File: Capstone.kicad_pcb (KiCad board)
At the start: 2 copper layers, 21 parts, among them U1 XIAO-ESP32-S3-DIP, U11 SN74HC161DR, U3 74LS151

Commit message: Redo Base Project file add code
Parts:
- removed C1: C, Capacitor_SMD:CP_Elec_3x5.3
- removed R1, R10, R11, R12, R13, R14, R15, R16, R17, R2, R3, R4, R5, R6, R7, R8, R9: R, Resistor_SMD:R_0201_0603Metric_Pad0.64x0.40mm_HandSolder
- removed U11: SN74HC161DR, CapstoneFootprints:D16
- added Cf1: 10p, Capacitor_THT:C_Disc_D3.8mm_W2.6mm_P2.50mm, F.Cu at (153.3, 105.8)
- added Cf2: 10p, Capacitor_THT:C_Disc_D3.8mm_W2.6mm_P2.50mm, F.Cu at (153.3, 110.0)
- added Cf3: 10p, Capacitor_THT:C_Disc_D3.8mm_W2.6mm_P2.50mm, F.Cu at (161.0, 105.8)
- added Cf4: 10p, Capacitor_THT:C_Disc_D3.8mm_W2.6mm_P2.50mm, F.Cu at (161.0, 110.0)
- added Ra1: 100k, Resistor_THT:R_Axial_DIN0204_L3.6mm_D1.6mm_P5.08mm_Horizontal, F.Cu at (142.3, 70.4)
- added Ra2: 100k, Resistor_THT:R_Axial_DIN0204_L3.6mm_D1.6mm_P5.08mm_Horizontal, F.Cu at (142.3, 92.3)
- added Rb1: 100k, Resistor_THT:R_Axial_DIN0204_L3.6mm_D1.6mm_P5.08mm_Horizontal, F.Cu at (142.3, 73.6)
- added Rb2: 100k, Resistor_THT:R_Axial_DIN0204_L3.6mm_D1.6mm_P5.08mm_Horizontal, F.Cu at (142.3, 95.4)
- added Rc1: 100k, Resistor_THT:R_Axial_DIN0204_L3.6mm_D1.6mm_P5.08mm_Horizontal, F.Cu at (142.3, 76.7)
- added Rc2: 100k, Resistor_THT:R_Axial_DIN0204_L3.6mm_D1.6mm_P5.08mm_Horizontal, F.Cu at (142.3, 98.6)
- added Rd1: 100k, Resistor_THT:R_Axial_DIN0204_L3.6mm_D1.6mm_P5.08mm_Horizontal, F.Cu at (142.3, 79.9)
- added Rd2: 100k, Resistor_THT:R_Axial_DIN0204_L3.6mm_D1.6mm_P5.08mm_Horizontal, F.Cu at (142.3, 101.7)
- added Rf1: 100k, Resistor_THT:R_Axial_DIN0204_L3.6mm_D1.6mm_P5.08mm_Horizontal, F.Cu at (142.3, 83.0)
- added Rf2: 100k, Resistor_THT:R_Axial_DIN0204_L3.6mm_D1.6mm_P5.08mm_Horizontal, F.Cu at (142.3, 86.2)
- added Rf3: 100k, Resistor_THT:R_Axial_DIN0204_L3.6mm_D1.6mm_P5.08mm_Horizontal, F.Cu at (142.3, 104.9)
- added Rf4: 100k, Resistor_THT:R_Axial_DIN0204_L3.6mm_D1.6mm_P5.08mm_Horizontal, F.Cu at (142.3, 108.0)
- added U2: LM358, Package_DIP:DIP-8_W7.62mm, F.Cu at (150.4, 70.9)
- added U4: LM358, Package_DIP:DIP-8_W7.62mm, F.Cu at (150.4, 92.7)
- added U5: LM358, Package_DIP:DIP-8_W7.62mm, F.Cu at (161.2, 92.7)
- U3: value 74LS151 -> LM358; footprint CapstoneFootprints:D16 -> Package_DIP:DIP-8_W7.62mm
- moved U3 15.1 mm to (161.2, 70.9)
- moved U1 6.13 mm to (184.0, 80.5), turned to 90 degrees
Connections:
- U1 pad 1: /Filter/Vout -> /SensorReader/Vout
- U1 pad 13: GND -> /SensorReader/Vref
- U1 pad 14: /8xAmplifier/V+ -> /SensorReader/V+
- U1 pad 2: unconnected-(U1-GPIO2_A1_D1-Pad2) -> /SensorReader1/Vout
- U1 pad 6: Net-(U1-GPIO6_A5_D5_SCL) -> unconnected-(U1-GPIO6_A5_D5_SCL-Pad6)
- U3 pad 1: /8xAmplifier/Vout4 -> /SensorReader1/Vout
- U3 pad 2: /8xAmplifier/Vout3 -> Net-(U3A--)
- U3 pad 3: /8xAmplifier/Vout2 -> Net-(U3A-+)
- U3 pad 4: /8xAmplifier/Vout1 -> /SensorReader/V-
- U3 pad 5: /Filter/Vin -> unconnected-(U3B-+-Pad5)
- U3 pad 8: GND -> /SensorReader/V+

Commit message: PCB designed rev1.0
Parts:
- removed Ra1, Ra2, Rb1, Rb2, Rd1, Rd2: 100k, Resistor_THT:R_Axial_DIN0204_L3.6mm_D1.6mm_P5.08mm_Horizontal
- added BT1: Battery, Connector_JST:JST_SUR_BM02B-SURS-TF_1x02-1MP_P0.80mm_Vertical, F.Cu at (176.7, 125.5)
- added C1: 100p, Capacitor_THT:C_Disc_D3.8mm_W2.6mm_P2.50mm, F.Cu at (95.6, 120.5)
- added C10: 1uF, Capacitor_THT:C_Disc_D3.8mm_W2.6mm_P2.50mm, F.Cu at (172.1, 105.4)
- added C11: 2.2uF, Capacitor_THT:C_Disc_D3.8mm_W2.6mm_P2.50mm, F.Cu at (166.8, 99.5)
- added C12: 100nF, Capacitor_THT:C_Disc_D3.8mm_W2.6mm_P2.50mm, F.Cu at (186.0, 126.2)
- added C13: 100p, Capacitor_THT:C_Disc_D3.8mm_W2.6mm_P2.50mm, F.Cu at (91.4, 123.7)
- added C14: 100p, Capacitor_THT:C_Disc_D3.8mm_W2.6mm_P2.50mm, F.Cu at (86.6, 123.7)
- added C16: 100p, Capacitor_THT:C_Disc_D3.8mm_W2.6mm_P2.50mm, F.Cu at (95.7, 103.7)
- added C17: 100p, Capacitor_THT:C_Disc_D3.8mm_W2.6mm_P2.50mm, F.Cu at (91.4, 106.9)
- added C18: 100p, Capacitor_THT:C_Disc_D3.8mm_W2.6mm_P2.50mm, F.Cu at (86.6, 106.9)
- added C19: 10uF, Capacitor_THT:C_Disc_D3.8mm_W2.6mm_P2.50mm, F.Cu at (177.4, 117.2)
- added C3: 3900pF, Capacitor_THT:C_Disc_D3.8mm_W2.6mm_P2.50mm, F.Cu at (177.4, 106.8)
- added C4: 10pF, Capacitor_THT:C_Disc_D3.8mm_W2.6mm_P2.50mm, F.Cu at (174.9, 120.6)
- added C5: 4.7uF, Capacitor_THT:C_Disc_D3.8mm_W2.6mm_P2.50mm, F.Cu at (147.9, 118.4)
- added C6: 10uF, Capacitor_THT:C_Disc_D3.8mm_W2.6mm_P2.50mm, F.Cu at (186.0, 121.5)
- added C7: 1uF, Capacitor_THT:C_Disc_D3.8mm_W2.6mm_P2.50mm, F.Cu at (179.8, 110.2)
- added C8: 10nF, Capacitor_THT:C_Disc_D3.8mm_W2.6mm_P2.50mm, F.Cu at (179.8, 106.8)
- added C9: 10uF, Capacitor_THT:C_Disc_D3.8mm_W2.6mm_P2.50mm, F.Cu at (186.0, 114.2)
- added D1: LED, LED_THT:LED_D3.0mm_Horizontal_O1.27mm_Z6.0mm, F.Cu at (163.9, 120.8)
- added D2: LED, LED_THT:LED_D3.0mm_Horizontal_O1.27mm_Z6.0mm, F.Cu at (169.9, 120.8)
- added D3: 1N34A, Diode_THT:D_DO-35_SOD27_P2.54mm_Vertical_AnodeUp, F.Cu at (96.7, 124.0)
- added D4: 1N34A, Diode_THT:D_DO-35_SOD27_P2.54mm_Vertical_AnodeUp, F.Cu at (96.7, 107.2)
- added D5: B240A, Diode_SMD:D_SMA, F.Cu at (178.6, 98.4)
- added J1: USB_C_Receptacle_PowerOnly_6P, Connector_USB:USB_C_Receptacle_GCT_USB4135-GF-A_6P_TopMnt_Horizontal, F.Cu at (156.0, 124.4)
- added L1: 3.9uH, Inductor_SMD:L_Bourns-SRN4018, F.Cu at (181.2, 121.2)
- added R1: 4.75k, Resistor_THT:R_Axial_DIN0204_L3.6mm_D1.6mm_P5.08mm_Horizontal, F.Cu at (174.9, 109.4)
- added R10: 1k, Resistor_THT:R_Axial_DIN0204_L3.6mm_D1.6mm_P5.08mm_Horizontal, F.Cu at (186.4, 111.9)
- added R11: 1k, Resistor_THT:R_Axial_DIN0204_L3.6mm_D1.6mm_P5.08mm_Horizontal, F.Cu at (142.8, 120.6)
- added R12: 500, Resistor_THT:R_Axial_DIN0204_L3.6mm_D1.6mm_P5.08mm_Horizontal, F.Cu at (111.4, 120.6)
- added R13: 500, Resistor_THT:R_Axial_DIN0204_L3.6mm_D1.6mm_P5.08mm_Horizontal, F.Cu at (111.4, 103.8)
- added R14: 1k, Resistor_THT:R_Axial_DIN0204_L3.6mm_D1.6mm_P5.08mm_Horizontal, F.Cu at (142.9, 103.8)
- added R15: 100R, Resistor_THT:R_Axial_DIN0204_L3.6mm_D1.6mm_P5.08mm_Horizontal, F.Cu at (186.4, 104.7)
- added R2: 33.2K, Resistor_THT:R_Axial_DIN0204_L3.6mm_D1.6mm_P5.08mm_Horizontal, F.Cu at (177.2, 114.6)
- added R3: 5.11k, Resistor_THT:R_Axial_DIN0204_L3.6mm_D1.6mm_P5.08mm_Horizontal, F.Cu at (157.9, 118.4)
- added R4: 5.11k, Resistor_THT:R_Axial_DIN0204_L3.6mm_D1.6mm_P5.08mm_Horizontal, F.Cu at (147.8, 121.3)
- added R5: 102k, Resistor_THT:R_Axial_DIN0204_L3.6mm_D1.6mm_P5.08mm_Horizontal, F.Cu at (173.8, 102.7)
- added R6: 1, Resistor_THT:R_Axial_DIN0204_L3.6mm_D1.6mm_P5.08mm_Horizontal, F.Cu at (179.8, 117.9)
- added R7: 5.11k, Resistor_THT:R_Axial_DIN0204_L3.6mm_D1.6mm_P5.08mm_Horizontal, F.Cu at (163.7, 118.0)
- added R8: 5.11k, Resistor_THT:R_Axial_DIN0204_L3.6mm_D1.6mm_P5.08mm_Horizontal, F.Cu at (171.0, 118.2)
- added R9: 5.11k, Resistor_THT:R_Axial_DIN0204_L3.6mm_D1.6mm_P5.08mm_Horizontal, F.Cu at (171.0, 111.0)
- added Rc3: 1k, Resistor_THT:R_Axial_DIN0204_L3.6mm_D1.6mm_P5.08mm_Horizontal, F.Cu at (92.6, 120.5)
- added Rc4: 100k, Resistor_THT:R_Axial_DIN0204_L3.6mm_D1.6mm_P5.08mm_Horizontal, F.Cu at (90.2, 115.5)
- added Rc5: 1k, Resistor_THT:R_Axial_DIN0204_L3.6mm_D1.6mm_P5.08mm_Horizontal, F.Cu at (87.8, 115.5)
- added Rc6: 1k, Resistor_THT:R_Axial_DIN0204_L3.6mm_D1.6mm_P5.08mm_Horizontal, F.Cu at (92.7, 103.7)
- added Rc7: 100k, Resistor_THT:R_Axial_DIN0204_L3.6mm_D1.6mm_P5.08mm_Horizontal, F.Cu at (90.3, 98.7)
- added Rc8: 1k, Resistor_THT:R_Axial_DIN0204_L3.6mm_D1.6mm_P5.08mm_Horizontal, F.Cu at (87.9, 98.7)
- added U10: ~, Package_TO_SOT_SMD:SOT-23-6, F.Cu at (182.6, 116.7)
- added U12: LM358, Package_DIP:DIP-8_W7.62mm, F.Cu at (131.7, 99.3)
- added U13: INA128, Package_DIP:DIP-8_W7.62mm, F.Cu at (101.5, 99.2)
- added U6: ADP1613ARMZ-R7, Package_SO:MSOP-8_3x3mm_P0.65mm, F.Cu at (178.6, 103.4)
- added U7: ~, Package_TO_SOT_SMD:SOT-23-8, F.Cu at (167.4, 115.0)
- added U8: LM2776, Package_TO_SOT_SMD:SOT-23-6, F.Cu at (170.6, 100.0)
- added U9: ~, Package_TO_SOT_SMD:SOT-23-6, F.Cu at (181.8, 125.8)
- Cf1, Cf3: value 10p -> 2p
- U3: value LM358 -> INA128
- moved U3 74.9 mm to (101.4, 116.0)
- moved Rc1 61.5 mm to (99.0, 120.5), turned to 90 degrees
- moved Cf3 52.7 mm to (111.4, 123.7)
- moved U2 43.9 mm to (116.9, 99.2)
- moved Rc2 43.5 mm to (99.1, 103.7), turned to 90 degrees
- moved Cf1 42.0 mm to (111.4, 106.9)
- moved U4 40.9 mm to (116.8, 116.0)
- moved U1 38.5 mm to (155.2, 106.0)
- moved U5 37.7 mm to (131.6, 116.1)
- moved Rf1 35.2 mm to (113.9, 103.8), turned to 90 degrees
- moved Cf4 34.7 mm to (126.8, 116.1)
- moved Rf3 32.5 mm to (113.8, 120.6), turned to 90 degrees
- moved Cf2 28.6 mm to (126.8, 99.3)
- moved Rf2 25.5 mm to (128.1, 107.3), turned to 90 degrees
- moved Rf4 21.5 mm to (128.0, 124.1), turned to 90 degrees
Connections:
- net /SensorReader/V- renamed -5V_OUT
- Rc1 pad 1: Net-(U3A--) -> Net-(D3-K)
- Rc1 pad 2: /SensorReader1/Vout -> Net-(Rc1-Pad2)
- Rc2 pad 1: Net-(U5A--) -> Net-(D4-K)
- Rc2 pad 2: /SensorReader/Vout -> Net-(Rc2-Pad2)
- U1 pad 13: /SensorReader/Vref -> GND
- U1 pad 14: /SensorReader/V+ -> 5V OUT
- U2 pad 3: /SensorReader/Vref -> GND
- U2 pad 5: /SensorReader/Vref -> GND
- U2 pad 8: /SensorReader/V+ -> 5V OUT
- U3 pad 1: /SensorReader1/Vout -> Net-(R12-Pad1)
- U3 pad 2: Net-(U3A--) -> /SensorReader/V2
- U3 pad 3: Net-(U3A-+) -> /SensorReader/V1
- U3 pad 5: unconnected-(U3B-+-Pad5) -> GND
- U3 pad 6: unconnected-(U3B---Pad6) -> Net-(D3-A)
- U3 pad 7: unconnected-(U3-Pad7) -> 5V OUT
- U3 pad 8: /SensorReader/V+ -> Net-(R12-Pad2)
- U4 pad 3: /SensorReader/Vref -> GND
- U4 pad 5: /SensorReader/Vref -> GND
- U4 pad 8: /SensorReader/V+ -> 5V OUT
- U5 pad 1: /SensorReader/Vout -> (no net)
- U5 pad 2: Net-(U5A--) -> (no net)
- U5 pad 3: Net-(U5A-+) -> (no net)
- U5 pad 5: unconnected-(U5B-+-Pad5) -> Net-(U5B-+)
- U5 pad 6: unconnected-(U5B---Pad6) -> Net-(U5B--)
- U5 pad 7: unconnected-(U5-Pad7) -> /SensorReader/Vout
- U5 pad 8: /SensorReader/V+ -> 5V OUT
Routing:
- net 5V OUT: track 0.00 -> 214.8 mm, vias 0 -> 18
- net -5V_OUT: track 0.00 -> 143.0 mm, vias 0 -> 11
- net Net-(U5B-+): track 0.00 -> 72.5 mm, vias 0 -> 4
- net Net-(U12B-+): track 0.00 -> 72.5 mm, vias 0 -> 4
- net Net-(D1-A): track 0.00 -> 53.0 mm, vias 0 -> 5
- net B+: track 0.00 -> 51.6 mm, vias 0 -> 3
- net /SensorReader1/V2: track 0.00 -> 42.6 mm, vias 0 -> 4
- net /SensorReader/V2: track 0.00 -> 42.6 mm, vias 0 -> 4
- net /SensorReader1/V1: track 0.00 -> 36.8 mm, vias 0 -> 5
- net /SensorReader/V1: track 0.00 -> 36.8 mm, vias 0 -> 5
- net /SensorReader/Vout: track 0.00 -> 33.0 mm, vias 0 -> 5
- net Net-(D5-A): track 0.00 -> 29.0 mm, vias 0 -> 2
- net Net-(U9-VCC): track 0.00 -> 27.2 mm, vias 0 -> 2
- net Net-(U6-COMP): track 0.00 -> 22.8 mm, vias 0 -> 2
- net Net-(U9-CS): track 0.00 -> 20.9 mm, vias 0 -> 4
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- added copper zone on B.Cu, net GND
- added copper zone on F.Cu, net GND
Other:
- board text added: "${REFERENCE}"

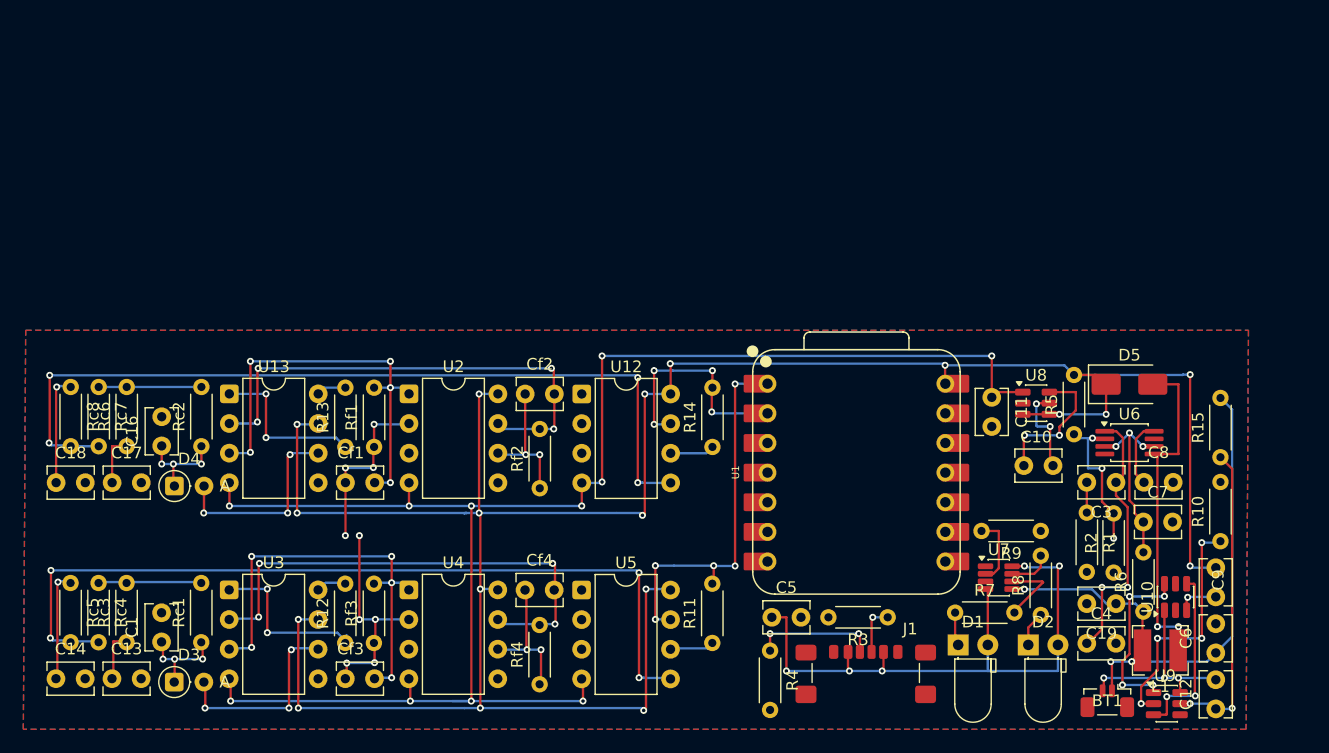
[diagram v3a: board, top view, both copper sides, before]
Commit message: Remove extra ref sensor
each module had a reference sensor before, now have single ref sensor comparing to both sensors
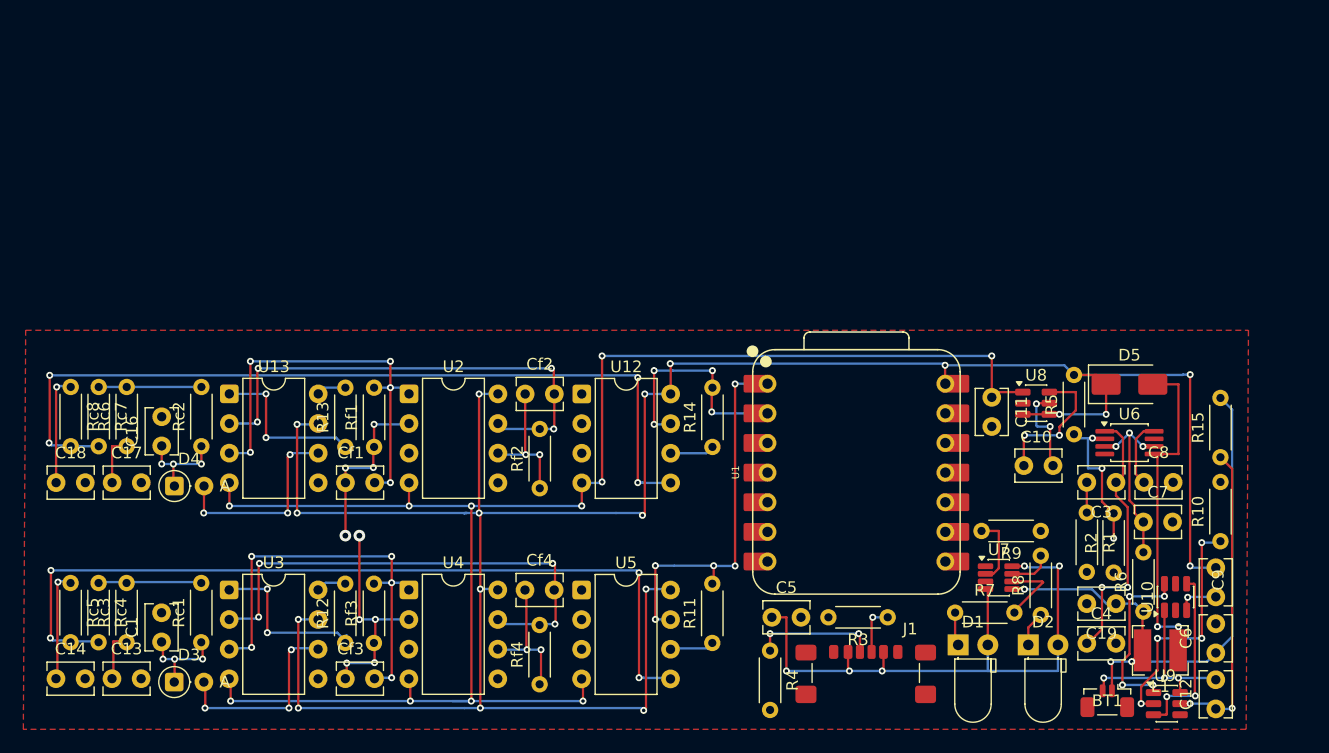
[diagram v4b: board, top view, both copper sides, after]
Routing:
- removed copper zone on B.Cu, net GND
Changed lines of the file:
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@@
 		)
 		(property "Value" "~"
-			(at 0 2.4 0)
+			(at 0.2 1.6 0)
 			(layer "F.Fab")
 			(effects
@@
 	(via
 		(at 111.4 111.4)
-		(size 0.6)
-		(drill 0.3)
+		(size 1)
+		(drill 0.5)
 		(layers "F.Cu" "B.Cu")
 		(net 1)
@@
 	(via
 		(at 112.6 111.4)
-		(size 0.6)
-		(drill 0.3)
+		(size 1)
+		(drill 0.5)
 		(layers "F.Cu" "B.Cu")
 		(net 24)
@@
 	)
 	(zone
+		(net 31)
+		(net_name "GND")
+		(layer "F.Cu")
+		(hatch edge 0.5)
+		(connect_pads
+			(clearance 0)
+		)
+		(min_thickness 0.25)
+		(filled_areas_thickness no)
+		(fill yes
+			(thermal_gap 0.5)
+			(thermal_bridge_width 0.5)
+		)
+		(polygon
+			(pts
+				(xy 84 93.8) (xy 188.8 93.8) (xy 188.6 128) (xy 83.8 128)
+			)
+		)
+	)
+	(zone
 		(net 0)
 		(net_name "")
@@
 			)
 		)
-	)
-	(zone
-		(net 31)
-		(net_name "GND")
-		(layers "F.Cu" "B.Cu")
-		(hatch edge 0.5)
-		(connect_pads
-			(clearance 0)
-		)
-		(min_thickness 0.25)
-		(filled_areas_thickness no)
-		(fill yes
-			(thermal_gap 0.5)
-			(thermal_bridge_width 0.5)
-		)
-		(polygon
-			(pts
-				(xy 84 93.8) (xy 188.8 93.8) (xy 188.6 128) (xy 83.8 128)
-			)
-		)

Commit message: Revert "Remove extra ref sensor"
This reverts commit 7f0b0207ac24b991faee57c630f393e10dd69dda.
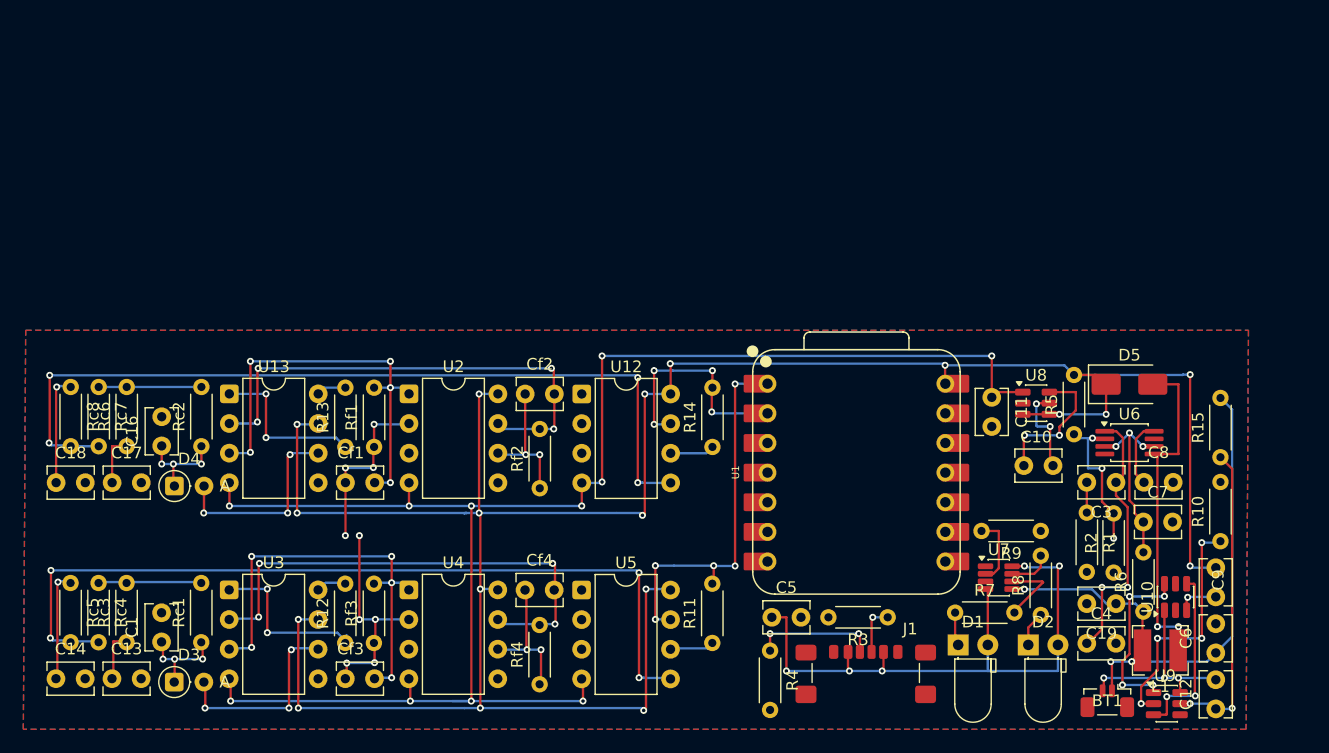
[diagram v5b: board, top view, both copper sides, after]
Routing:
- added copper zone on B.Cu, net GND
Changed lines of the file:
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@@
 		)
 		(property "Value" "~"
-			(at 0.2 1.6 0)
+			(at 0 2.4 0)
 			(layer "F.Fab")
 			(effects
@@
 	(via
 		(at 111.4 111.4)
-		(size 1)
-		(drill 0.5)
+		(size 0.6)
+		(drill 0.3)
 		(layers "F.Cu" "B.Cu")
 		(net 1)
@@
 	(via
 		(at 112.6 111.4)
-		(size 1)
-		(drill 0.5)
+		(size 0.6)
+		(drill 0.3)
 		(layers "F.Cu" "B.Cu")
 		(net 24)
@@
 	)
 	(zone
-		(net 31)
-		(net_name "GND")
-		(layer "F.Cu")
-		(hatch edge 0.5)
-		(connect_pads
-			(clearance 0)
-		)
-		(min_thickness 0.25)
-		(filled_areas_thickness no)
-		(fill yes
-			(thermal_gap 0.5)
-			(thermal_bridge_width 0.5)
-		)
-		(polygon
-			(pts
-				(xy 84 93.8) (xy 188.8 93.8) (xy 188.6 128) (xy 83.8 128)
-			)
-		)
-	)
-	(zone
 		(net 0)
 		(net_name "")
@@
 			)
 		)
+	)
+	(zone
+		(net 31)
+		(net_name "GND")
+		(layers "F.Cu" "B.Cu")
+		(hatch edge 0.5)
+		(connect_pads
+			(clearance 0)
+		)
+		(min_thickness 0.25)
+		(filled_areas_thickness no)
+		(fill yes
+			(thermal_gap 0.5)
+			(thermal_bridge_width 0.5)
+		)
+		(polygon
+			(pts
+				(xy 84 93.8) (xy 188.8 93.8) (xy 188.6 128) (xy 83.8 128)
+			)
+		)
